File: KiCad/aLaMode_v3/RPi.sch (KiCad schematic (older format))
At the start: 9 parts, among them P1 BCM2835_GPIO, P11 U6_OE, P16 5V_LINK, P2 GPU_JTAG, P3 LAN_JTAG, U6 TXS0108

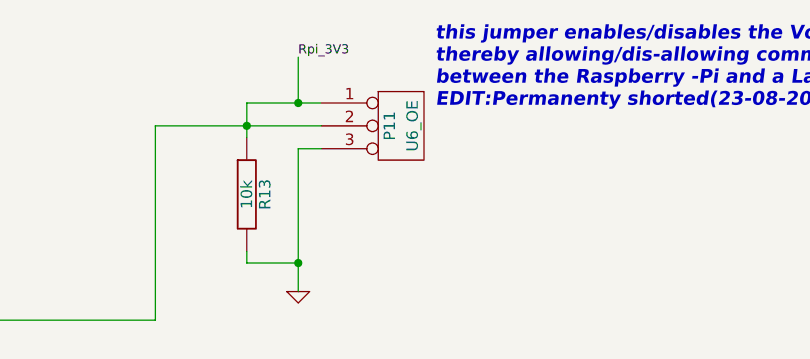
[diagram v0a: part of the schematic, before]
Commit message: AlaMode_v3 : Updated BOM. Added resistors for GPS Rx.
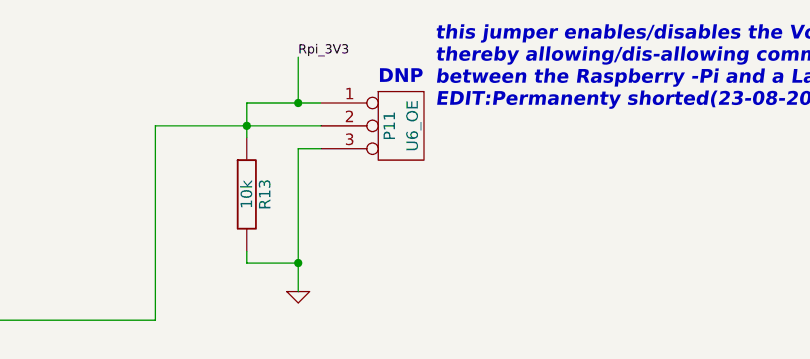
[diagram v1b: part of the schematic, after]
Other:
- note added: "DNP"
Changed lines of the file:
@@
-EESchema Schematic File Version 2  date 12-Jun-13 2:07:35 PM
+EESchema Schematic File Version 2  date 14-Jun-13 12:23:48 PM
 LIBS:aLaMode
 LIBS:Conn-raspberry
@@
 Sheet 4 4
 Title "aLaMode_v3"
-Date "12 jun 2013"
-Rev "1"
-Comp "WyoLum"
+Date "14 jun 2013"
+Rev "3"
+Comp "WyoLum :: http://wyolum.com/projects/alamode/"
 Comment1 ""
 Comment2 ""
@@
 Rpi_3V3
 $Comp
-L GND #PWR021
+L GND #PWR022
 U 1 1 4FD8C28A
 P 5850 2050
-F 0 "#PWR021" H 5850 2050 30  0001 C CNN
+F 0 "#PWR022" H 5850 2050 30  0001 C CNN
 F 1 "GND" H 5850 1980 30  0001 C CNN
 F 2 "" H 5850 2050 60  0001 C CNN
@@
 Rpi_3V3
 $Comp
-L GND #PWR022
+L GND #PWR023
 U 1 1 4FD62C0F
 P 2125 2175
-F 0 "#PWR022" H 2125 2175 30  0001 C CNN
+F 0 "#PWR023" H 2125 2175 30  0001 C CNN
 F 1 "GND" H 2125 2105 30  0001 C CNN
 F 2 "" H 2125 2175 60  0001 C CNN
@@
 $EndComp
 $Comp
-L GND #PWR023
+L GND #PWR024
 U 1 1 4FD62BFD
 P 2125 3600
-F 0 "#PWR023" H 2125 3600 30  0001 C CNN
+F 0 "#PWR024" H 2125 3600 30  0001 C CNN
 F 1 "GND" H 2125 3530 30  0001 C CNN
 F 2 "" H 2125 3600 60  0001 C CNN
@@
 $EndComp
 $Comp
-L PWR_FLAG #FLG024
+L PWR_FLAG #FLG025
 U 1 1 51B85026
 P 6300 3950
-F 0 "#FLG024" H 6300 4220 30  0001 C CNN
+F 0 "#FLG025" H 6300 4220 30  0001 C CNN
 F 1 "PWR_FLAG" H 6300 4180 30  0000 C CNN
 F 2 "" H 6300 3950 60  0000 C CNN
@@
 	6300 3950 6300 4100
 Connection ~ 6300 4100
+Text Notes 6200 1150 0    60   ~ 12
+DNP
 $EndSCHEMATC
